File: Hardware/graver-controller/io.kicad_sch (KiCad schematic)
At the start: 21 parts, among them J401 LCD 1x7, J402 NMJ6HCD2, SW401 EC11E15244G1, U401 PESD5V0S2BT

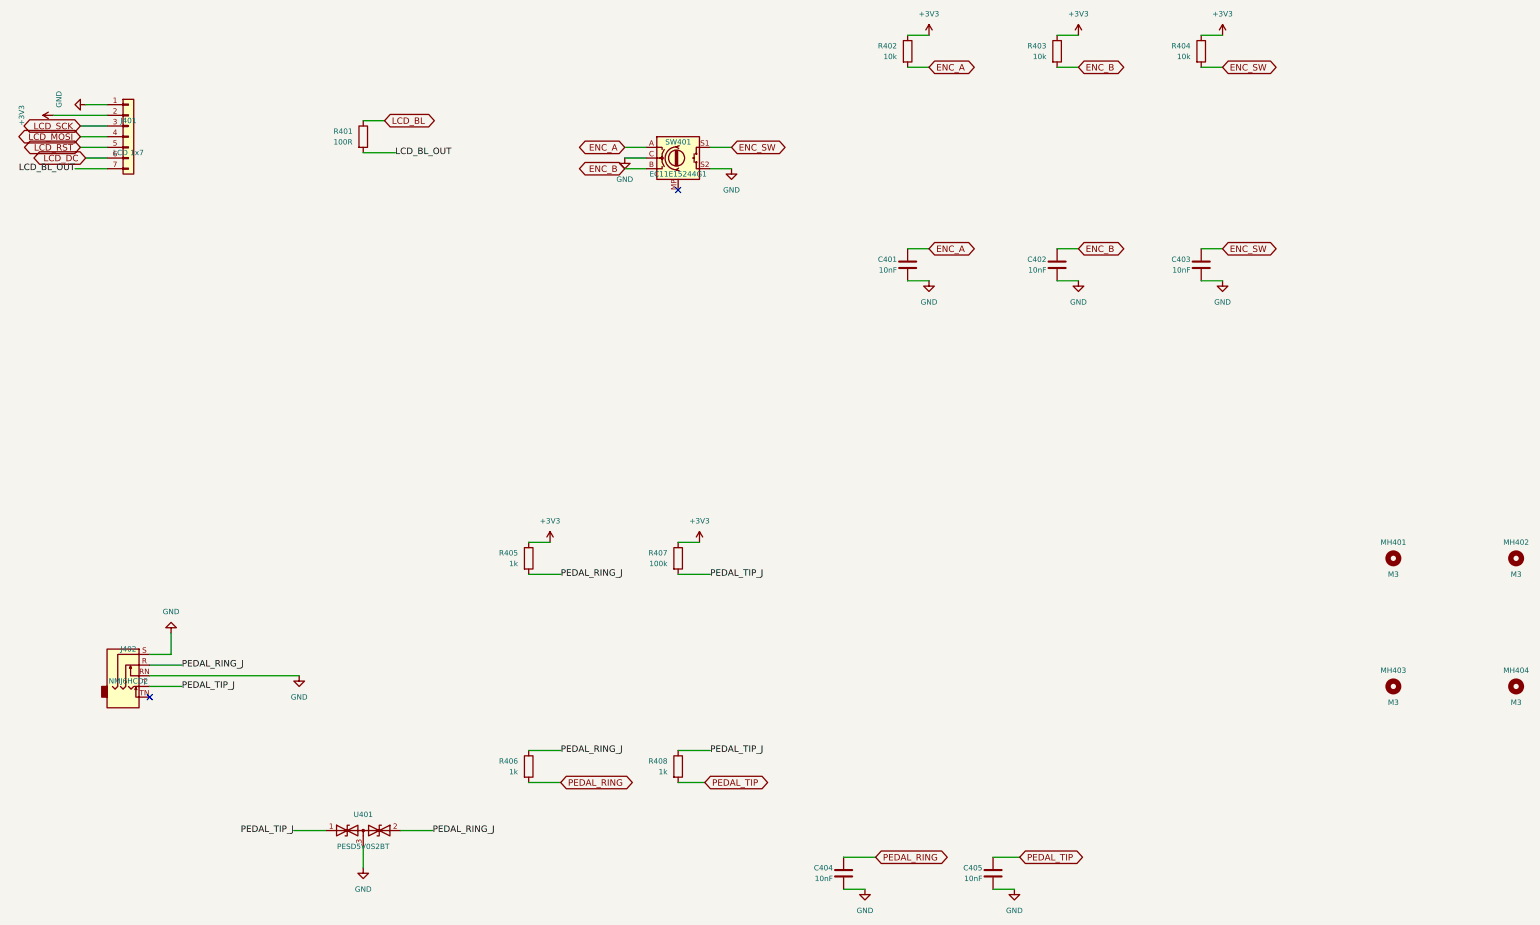
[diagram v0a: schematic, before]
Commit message: hardware: redraw the four schematic sheets with real wiring
The captured sheets connected everything by name with parts scattered on
the page. The sheets are now generated from hand-designed layouts
(Hardware/graver-controller/tools): decoupling caps drawn at their pins,
signal flow left to right, wires inside each block, global labels only
where a net crosses sheets. Power is two rows, MCU and IO fit A4.

Circuit unchanged: verify.sh compares the XML netlist against the
captured sheets kept in tools/ref (117 components with values,
footprints and LCSC fields, 65 nets by pin set) - identical. ERC: 0
violations. Q203 uses the generic Q_NMOS_GSD symbol (value BSS123),
which removes the library-mismatch warning.
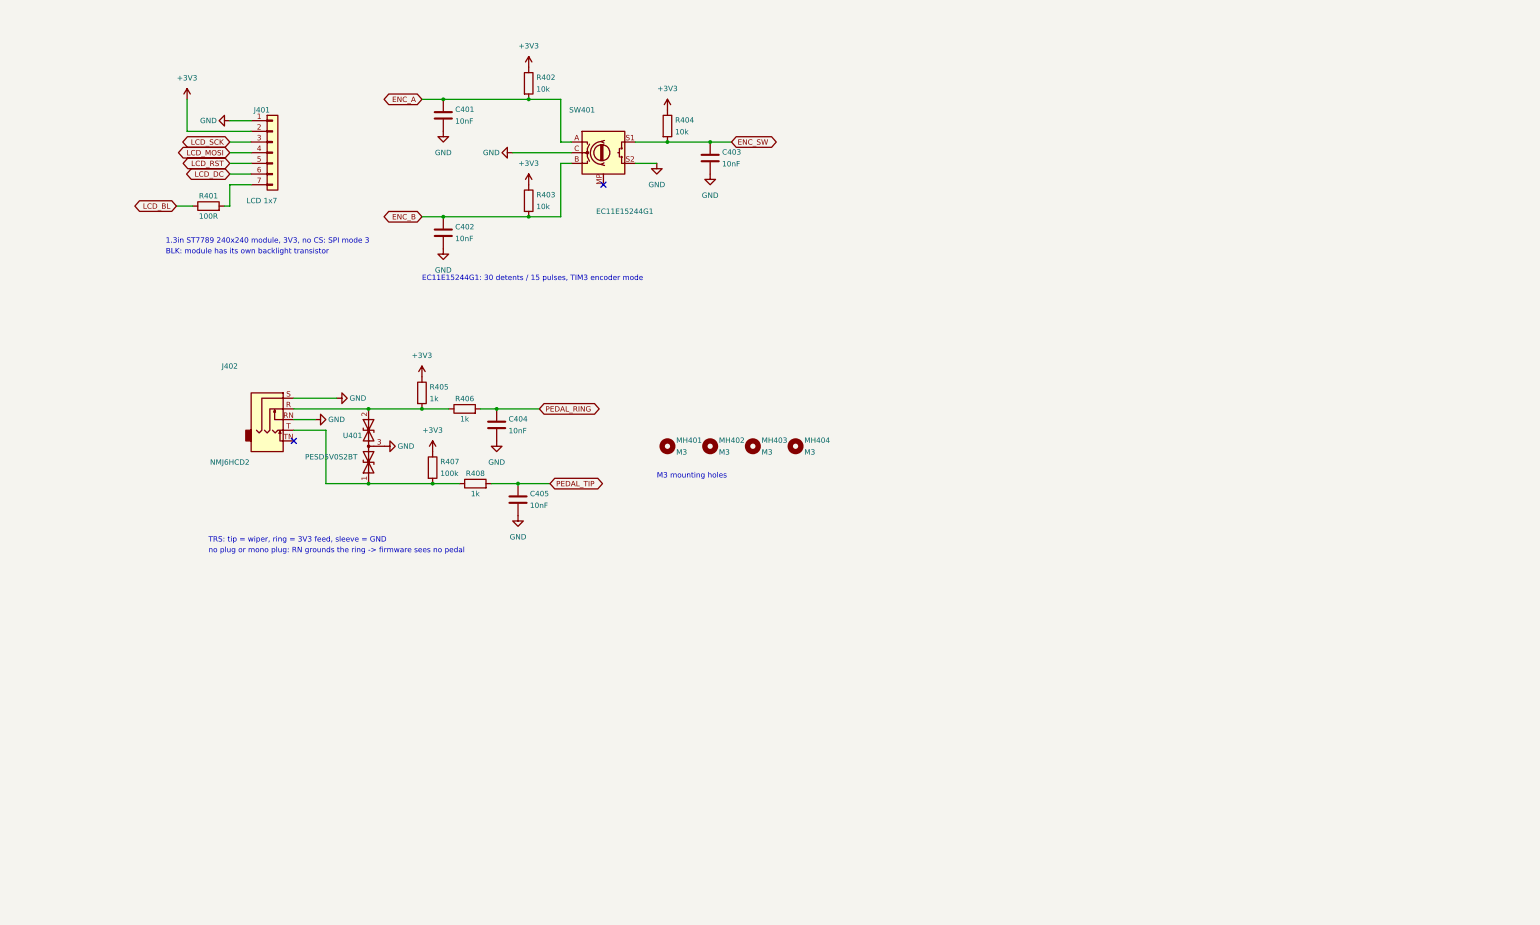
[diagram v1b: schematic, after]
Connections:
- net LCD_BL_OUT: no longer names the net of J401.7 (Pin_7), R401.2
- net PEDAL_RING_J: no longer names the net of J402.R, R405.2, R406.1, U401.2 (A2)
- net PEDAL_TIP_J: no longer names the net of J402.T, R407.2, R408.1, U401.1 (A1)
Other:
- note added: "1.3in ST7789 240x240 module, 3V3, no CS: SPI mode 3"
- note added: "BLK: module has its own backlight transistor"
- note added: "EC11E15244G1: 30 detents / 15 pulses, TIM3 encoder mode"
- note added: "M3 mounting holes"
- note added: "TRS: tip = wiper, ring = 3V3 feed, sleeve = GND"
- note added: "no plug or mono plug: RN grounds the ring -> firmware sees no pedal"
